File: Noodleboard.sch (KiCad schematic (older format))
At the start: 28 parts, among them CON1 SWD, IC1 LD1117S33, U1 STM32F405RGT6, X1 25 MHz

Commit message: #3 Add SD card interface #4 Add CAN & UART transceivers
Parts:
- removed C1, C2: 4.7p, ~, symbol C
- removed C10, C12: 2u2, ~, symbol CP1
- removed C11, C4, C5, C7, C8, C9: 100n, ~, symbol C
- removed C13, C6: 1u, ~, symbol C
- removed C14: 10u, ~, symbol CP1
- removed C3: 1u, ~, symbol CP1
- removed C32: 4u7, ~, symbol CP1
- removed CON1: SWD, symbol SWD
- removed D1: DIODE, ~, symbol DIODE
- removed F1: FUSE, ~, symbol FUSE
- removed IC1: LD1117S33, ~, symbol LD1117S33
- removed JP1: JUMPER, ~, symbol JUMPER
- removed L1: fcm1608, ~, symbol INDUCTOR
- removed R1, R2: 0, ~, symbol R
- removed R3: 47, ~, symbol R
- removed R4: 10k, ~, symbol R
- removed R5: 510, ~, symbol R
- removed U1: STM32F405RGT6, ~, symbol STM32F405RGT6
- removed X1: 25 MHz, ~, symbol CRYSTAL
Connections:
- net labels added: 5V0, AN_IO_1, AN_IO_2, AN_IO_3, AN_IO_4, AN_IO_5, BOOT_STATE, CAN_RX, CAN_TX, DAC_1, DIG_IO_1, DIG_IO_2, DIG_IO_3, DIG_IO_4, DIG_IO_5, DIG_IO_6, ENABLE_BOOT, I2C_SCL, I2C_SDA, SDIO_CK, SDIO_CMD, SDIO_D0, SDIO_D1, SDIO_D2, SDIO_D3, SDIO_SD_D, SPI_MISO, SPI_MOSI, SPI_NSS, SPI_SCK, UART_RX, UART_TX, USART_CK, USART_RX, USART_TX, ~RST
- net labels removed: 5V, A0, A1, A10, A11, A2, A3, A6, A7, A8, A9, GND_MCU, GPIO1, GPIO2, GPIO3, GPIO4, GPIO5, GPIO6, GPIO7, LED1, LED2, LED3, LED4, MISO, MOSI, NRST, NSS, PWM1, PWM2, PWM3, PWM4, RX, SCL, SCLK, SDA, TX, VBAT, VBUS_HS, VCAP_1, VCAP_2
- wire segments 176 -> 137
- no-connect marks 1 -> 0
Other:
- note added: "B2B"
- note added: "Boot & Reset\n"
- note added: "CAN"
- note added: "External Clocks"
- note added: "IO"
- note added: "MCU"
- note added: "SDIO (uSD)"
- note added: "UART\n"
- note removed: "0R resistor"
- note removed: "External Clock"
- note removed: "FIT A 0R RESISTOR"
- note removed: "IO Peripherals"
- note removed: "MCU\n\nSTMF405RG"

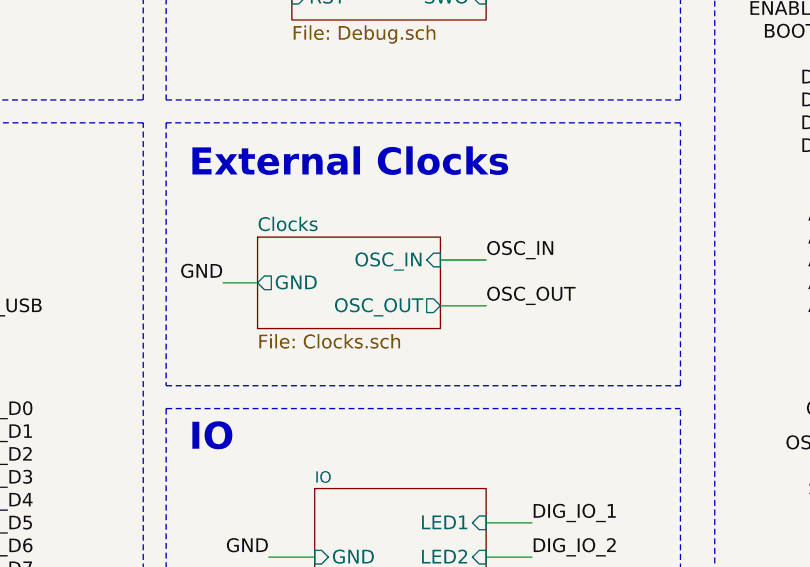
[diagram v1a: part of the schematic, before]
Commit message: - #4 Added UART and CAN interface transceivers - Improved schematic structure - Removed all gerber outputs - Generated schematics outputs for PCB design - Updated local libraries
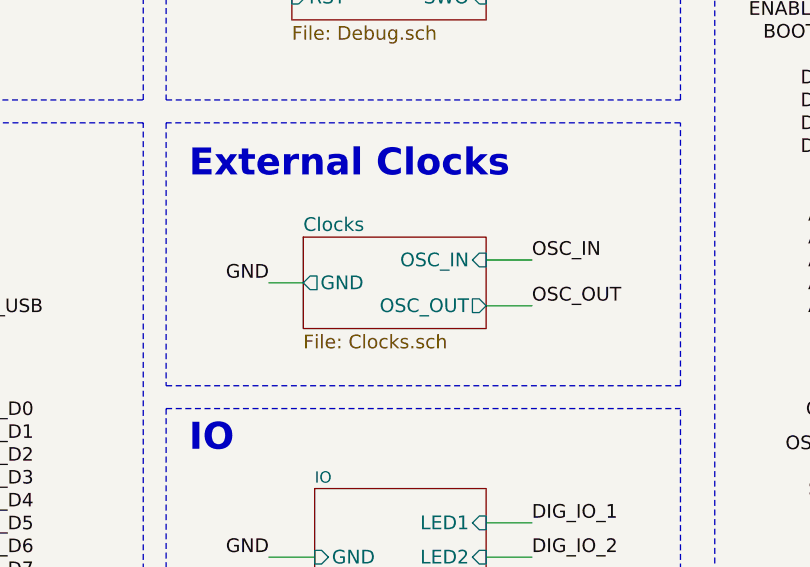
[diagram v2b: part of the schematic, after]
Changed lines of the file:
@@
 $EndSheet
 $Sheet
-S 6100 3950 800  400
+S 6300 3950 800  400
 U 56047B2D
 F0 "Clocks" 60
 F1 "Clocks.sch" 60
-F2 "GND" O L 6100 4150 60
-F3 "OSC_IN" I R 6900 4050 60
-F4 "OSC_OUT" O R 6900 4250 60
+F2 "GND" O L 6300 4150 60
+F3 "OSC_IN" I R 7100 4050 60
+F4 "OSC_OUT" O R 7100 4250 60
 $EndSheet
 Text Notes 700  1050 0    118  ~ 24
@@
 Wire Wire Line
 	8850 3100 9000 3100
-Text Label 5950 4150 2    60   ~ 0
-GND
-Wire Wire Line
-	5950 4150 6100 4150
-Text Label 7100 4050 0    60   ~ 0
+Text Label 6150 4150 2    60   ~ 0
+GND
+Wire Wire Line
+	6150 4150 6300 4150
+Text Label 7300 4050 0    60   ~ 0
 OSC_IN
-Text Label 7100 4250 0    60   ~ 0
+Text Label 7300 4250 0    60   ~ 0
 OSC_OUT
 Wire Wire Line
-	6900 4050 7100 4050
-Wire Wire Line
-	6900 4250 7100 4250
+	7100 4050 7300 4050
+Wire Wire Line
+	7100 4250 7300 4250
 Text Label 8800 4750 2    60   ~ 0
 OSC_IN
